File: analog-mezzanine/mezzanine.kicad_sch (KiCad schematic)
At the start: 16 parts, among them J1 Conn_Coaxial, J2 Conn_Coaxial, J9 LD15P24A4GV00LF

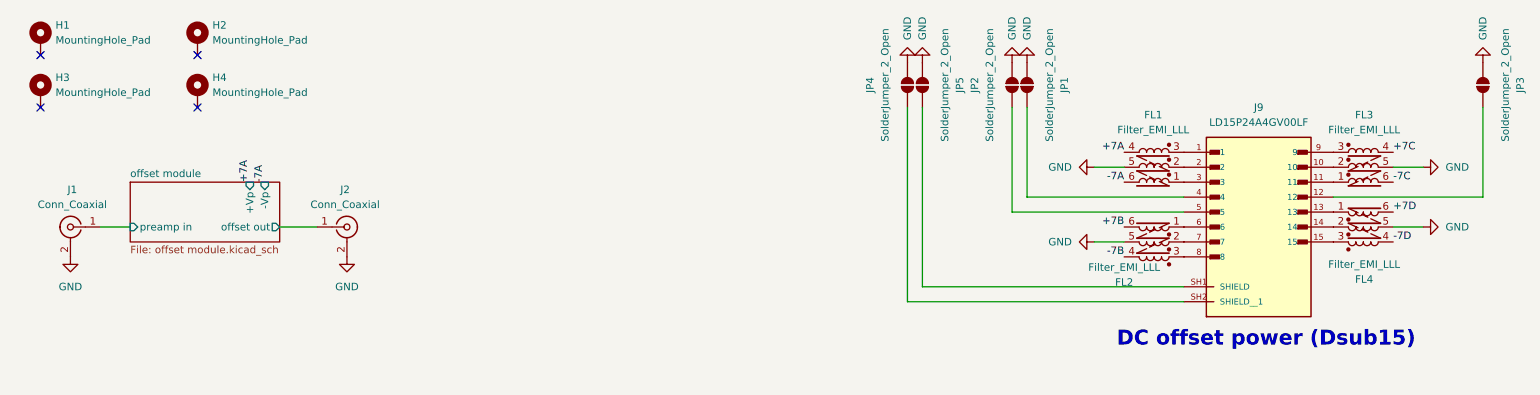
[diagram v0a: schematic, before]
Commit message: wire up linear regulators for offset
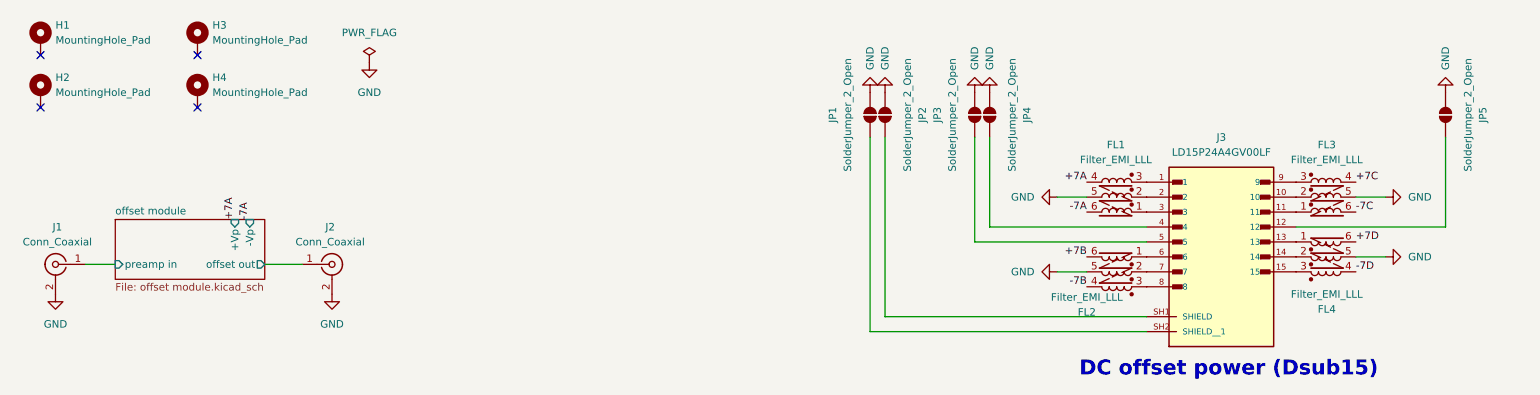
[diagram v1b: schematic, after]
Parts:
- renumbered H3 to H2, H2 to H3, J9 to J3, JP4 to JP1, JP5 to JP2, JP2 to JP3, JP1 to JP4, JP3 to JP5
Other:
- moved on the sheet: FL1, FL2, FL3, FL4, J1, J2, J3, JP1, JP2, JP3, JP4, JP5

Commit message: start layout
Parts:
- added J2, J3, J4: Conn_Coaxial, Connector_Coaxial:MMCX_Molex_73415-0961_Horizontal_1.0mm-PCB, symbol Connector:Conn_Coaxial
- added J6, J7, J8: Conn_Coaxial, Connector_Coaxial:MMCX_Molex_73415-1471_Vertical, symbol Connector:Conn_Coaxial
- J5: renamed from J2; footprint Connector_Coaxial:MMCX_Molex_73415-0961_Horizontal_1.0mm-PCB -> Connector_Coaxial:MMCX_Molex_73415-1471_Vertical
- JP1, JP2, JP3, JP4, JP5: footprint (none) -> Jumper:SolderJumper-2_P1.3mm_Open_RoundedPad1.0x1.5mm
- renumbered J3 to J9
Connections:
- net +7B: now also FL2.4 (2); no longer FL2.6
- net +7C: now also FL3.6; no longer FL3.4 (2)
- net -7B: now also FL2.6; no longer FL2.4 (2)
- net -7C: now also FL3.4 (2); no longer FL3.6
- net GND: now also J2.2 (Ext), J3.2 (Ext), J4.2 (Ext), J6.2 (Ext), J7.2 (Ext), J8.2 (Ext)
- net at FL3.1 (5): now also J9.9; no longer J9.11
- net at FL3.3 (1): now also J9.11; no longer J9.9
- net at FL2.1 (5): now also J9.8; no longer J9.6
- net at FL2.3 (1): now also J9.6; no longer J9.8
- new net offset module1/offset out: J6.1 (In)
- new net offset module1/preamp in: J2.1 (In)
- new net offset module2/offset out: J7.1 (In)
- new net offset module2/preamp in: J3.1 (In)
- new net offset module3/offset out: J8.1 (In)
- new net offset module3/preamp in: J4.1 (In)
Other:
- added sheet offset module1 (offset module.kicad_sch)
- added sheet offset module2 (offset module.kicad_sch)
- added sheet offset module3 (offset module.kicad_sch)
- moved on the sheet: FL2

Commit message: laid out chunks and power
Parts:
- J1, J2, J3, J4: footprint Connector_Coaxial:MMCX_Molex_73415-0961_Horizontal_1.0mm-PCB -> Connector_Coaxial:MMCX_Molex_73415-1471_Vertical

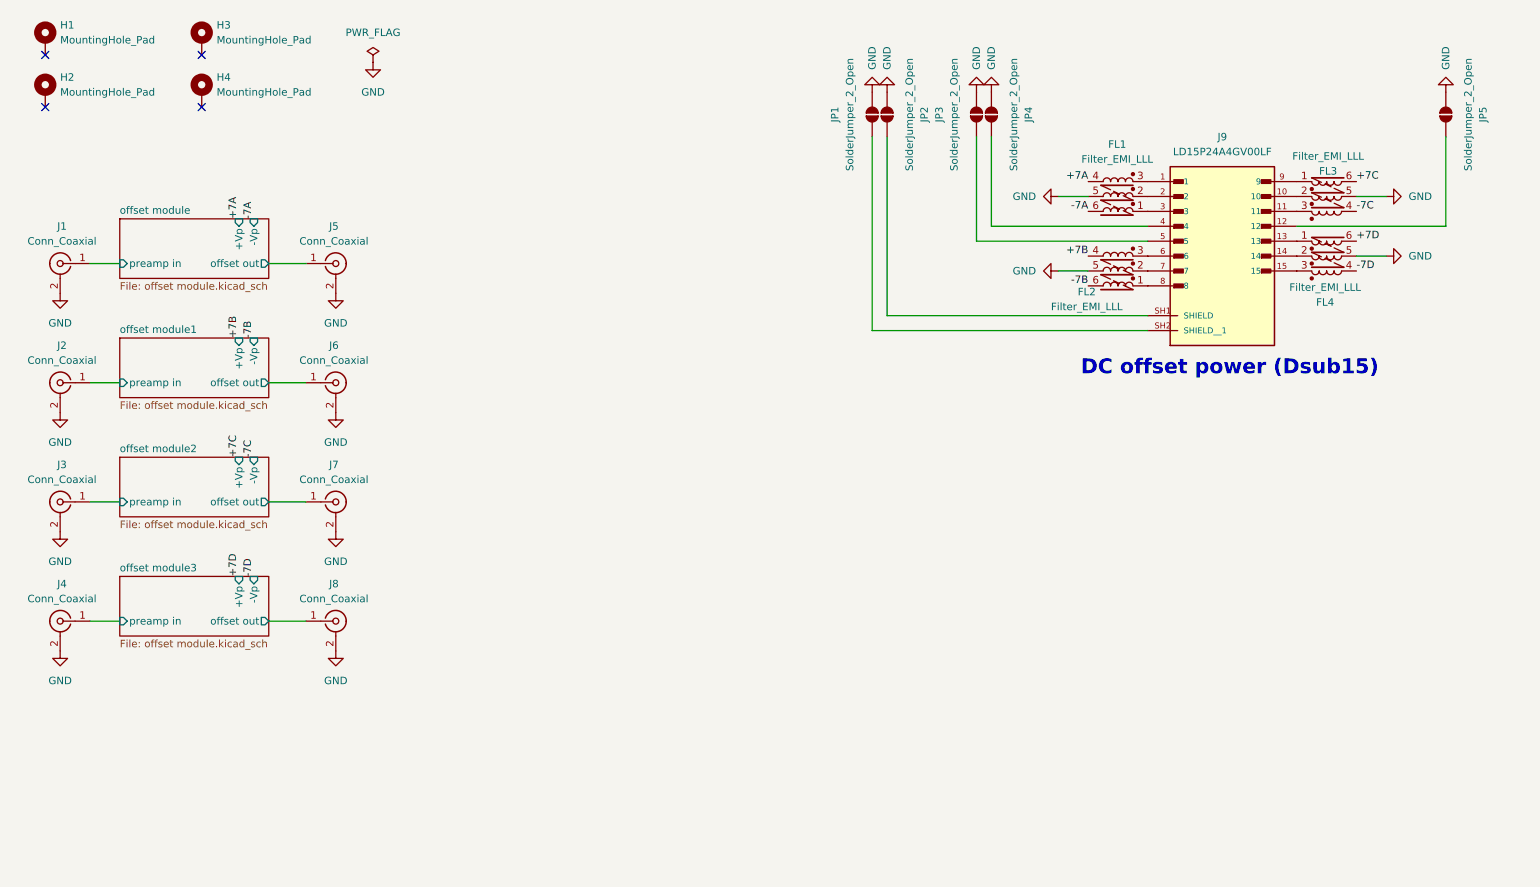
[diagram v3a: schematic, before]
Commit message: re-layout, better ground plane config
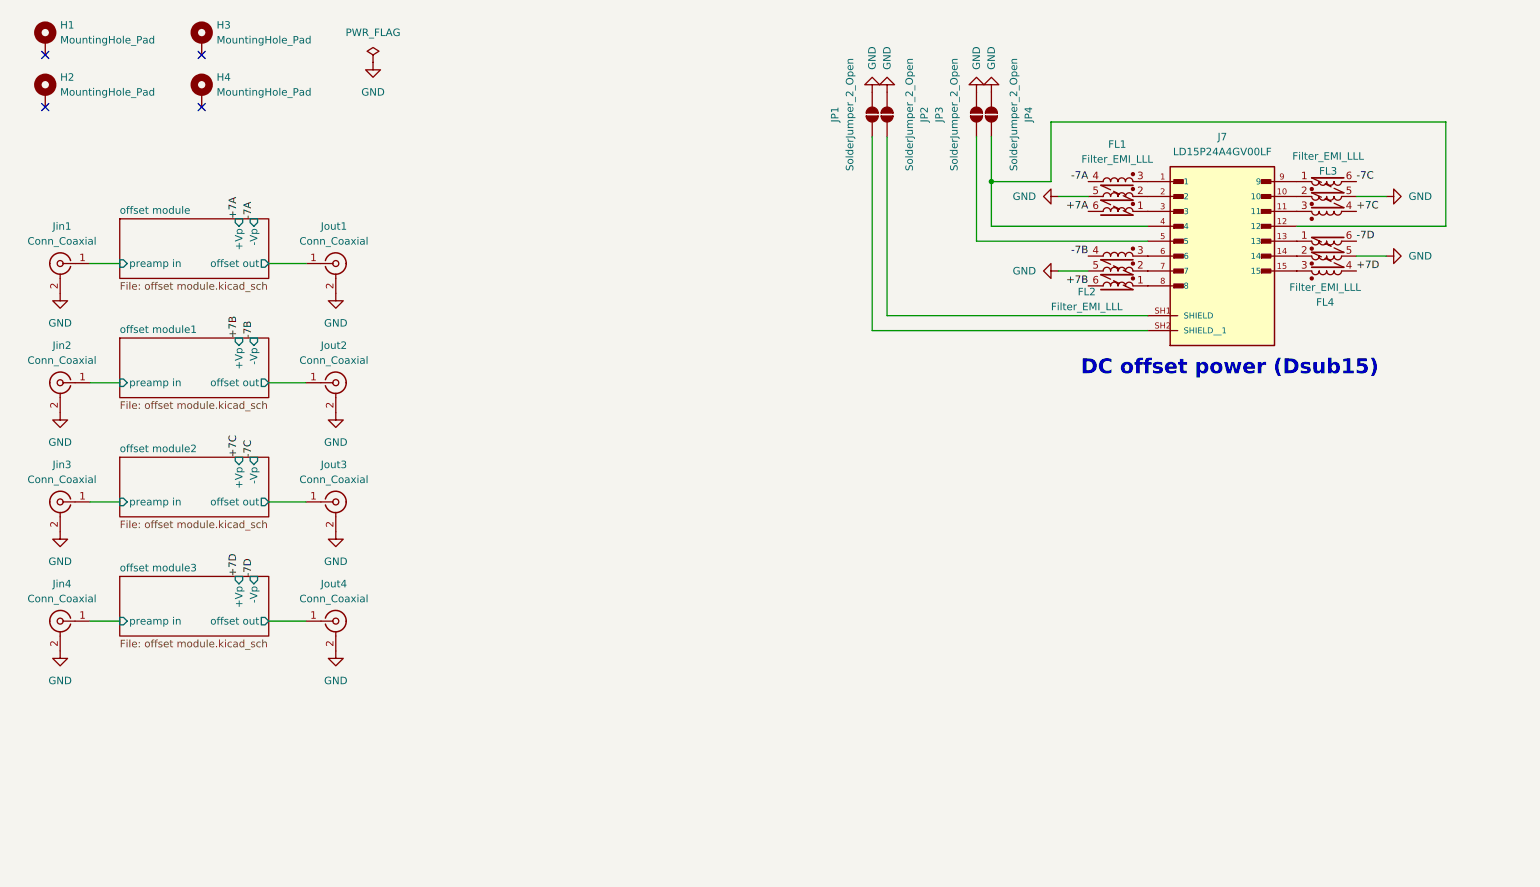
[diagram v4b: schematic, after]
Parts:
- removed JP5: SolderJumper_2_Open, Jumper:SolderJumper-2_P1.3mm_Open_RoundedPad1.0x1.5mm, symbol Jumper:SolderJumper_2_Open
- renumbered J9 to J7, J1 to Jin1, J2 to Jin2, J3 to Jin3, J4 to Jin4, J5 to Jout1, J6 to Jout2, J7 to Jout3, J8 to Jout4
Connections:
- net +7A: now also FL1.6; no longer FL1.4 (2)
- net +7B: now also FL2.6; no longer FL2.4 (2)
- net +7C: now also FL3.4 (2); no longer FL3.6
- net +7D: now also FL4.4 (2); no longer FL4.6
- net -7A: now also FL1.4 (2); no longer FL1.6
- net -7B: now also FL2.4 (2); no longer FL2.6
- net -7C: now also FL3.6; no longer FL3.4 (2)
- net -7D: now also FL4.6; no longer FL4.4 (2)
- net at J7.4, JP4.2 (B): now also J7.12
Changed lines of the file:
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@@
 		)
 	)
+	(junction
+		(at 189.23 45.72)
+		(diameter 0)
+		(color 0 0 0 0)
+	)
 	(no_connect
 		(at 27.94 33.02)
@@
 	(wire
 		(pts
+			(xy 266.7 35.56) (xy 199.39 35.56)
+		)
+		(stroke
+			(width 0)
+			(type default)
+		)
+	)
+	(wire
+		(pts
 			(xy 186.69 38.1) (xy 186.69 55.88)
 		)
@@
 	(wire
 		(pts
-			(xy 189.23 53.34) (xy 189.23 38.1)
+			(xy 189.23 53.34) (xy 189.23 45.72)
 		)
 		(stroke
@@
 	(wire
 		(pts
+			(xy 266.7 53.34) (xy 266.7 35.56)
+		)
+		(stroke
+			(width 0)
+			(type default)
+		)
+	)
+	(wire
+		(pts
+			(xy 189.23 45.72) (xy 189.23 38.1)
+		)
+		(stroke
+			(width 0)
+			(type default)
+		)
+	)
+	(wire
+		(pts
 			(xy 215.9 68.58) (xy 171.45 68.58)
 		)
@@
 	(wire
 		(pts
-			(xy 266.7 53.34) (xy 266.7 38.1)
+			(xy 199.39 45.72) (xy 189.23 45.72)
 		)
 		(stroke
@@
 	(wire
 		(pts
+			(xy 199.39 35.56) (xy 199.39 45.72)
+		)
+		(stroke
+			(width 0)
+			(type default)
+		)
+	)
+	(wire
+		(pts
 			(xy 200.66 48.26) (xy 205.74 48.26)
 		)
@@
 	)
 	(label "+7B"
-		(at 205.74 58.42 180)
+		(at 205.74 63.5 180)
 		(effects
 			(font
@@
 	)
 	(label "+7A"
-		(at 205.74 45.72 180)
+		(at 205.74 50.8 180)
 		(effects
 			(font
@@
 	)
 	(label "-7A"
-		(at 205.74 50.8 180)
+		(at 205.74 45.72 180)
 		(effects
 			(font
@@
 	)
 	(label "+7C"
-		(at 251.46 45.72 0)
+		(at 251.46 50.8 0)
 		(effects
 			(font
@@
 	)
 	(label "-7C"
-		(at 251.46 50.8 0)
+		(at 251.46 45.72 0)
 		(effects
 			(font
@@
 	)
 	(label "-7B"
-		(at 205.74 63.5 180)
+		(at 205.74 58.42 180)
 		(effects
 			(font
@@
 	)
 	(label "-7D"
-		(at 251.46 60.96 0)
+		(at 251.46 55.88 0)
 		(effects
 			(font
@@
 	)
 	(label "+7D"
-		(at 251.46 55.88 0)
+		(at 251.46 60.96 0)
 		(effects
 			(font
@@
 		(on_board yes)
 		(dnp no)
-		(property "Reference" "J5"
+		(property "Reference" "Jout1"
 			(at 77.1526 53.34 0)
 			(effects
@@
 			(project "dc-offsetter"
 				(path "/beaf6512-ab3f-4084-8005-c7f9afb6bef5"
-					(reference "J5")
+					(reference "Jout1")
 					(unit 1)
 				)
@@
 		(on_board yes)
 		(dnp no)
-		(property "Reference" "J4"
+		(property "Reference" "Jin4"
 			(at 30.7974 114.3 0)
 			(effects
@@
 			(project "mezzanine"
 				(path "/beaf6512-ab3f-4084-8005-c7f9afb6bef5"
-					(reference "J4")
+					(reference "Jin4")
 					(unit 1)
 				)
@@
 	)
 	(symbol
+		(lib_name "Filter_EMI_LLL_3")
 		(lib_id "Device:Filter_EMI_LLL")
 		(at 246.38 48.26 0)
@@
 		(on_board yes)
 		(dnp no)
-		(property "Reference" "J7"
+		(property "Reference" "Jout3"
 			(at 77.1526 93.98 0)
 			(effects
@@
 			(project "mezzanine"
 				(path "/beaf6512-ab3f-4084-8005-c7f9afb6bef5"
-					(reference "J7")
+					(reference "Jout3")
 					(unit 1)
 				)
@@
 		(on_board yes)
 		(dnp no)
-		(property "Reference" "J6"
+		(property "Reference" "Jout2"
 			(at 77.1526 73.66 0)
 			(effects
@@
 			(project "mezzanine"
 				(path "/beaf6512-ab3f-4084-8005-c7f9afb6bef5"
-					(reference "J6")
+					(reference "Jout2")
 					(unit 1)
 				)
@@
 		(on_board yes)
 		(dnp no)
-		(property "Reference" "J3"
+		(property "Reference" "Jin3"
 			(at 30.7974 93.98 0)
 			(effects
@@
 			(project "mezzanine"
 				(path "/beaf6512-ab3f-4084-8005-c7f9afb6bef5"
-					(reference "J3")
+					(reference "Jin3")
 					(unit 1)
 				)
@@
 	)
 	(symbol
+		(lib_name "Filter_EMI_LLL_2")
 		(lib_id "Device:Filter_EMI_LLL")
 		(at 210.82 60.96 0)
@@
 		(on_board yes)
 		(dnp no)
-		(property "Reference" "J1"
+		(property "Reference" "Jin1"
 			(at 30.7974 53.34 0)
 			(effects
@@
 			(project "mezzanine"
 				(path "/beaf6512-ab3f-4084-8005-c7f9afb6bef5"
-					(reference "J1")
+					(reference "Jin1")
 					(unit 1)
 				)
@@
 	)
 	(symbol
-		(lib_id "Jumper:SolderJumper_2_Open")
-		(at 266.7 34.29 90)
-		(mirror x)
-		(unit 1)
-		(exclude_from_sim no)
-		(in_bom no)
-		(on_board yes)
-		(dnp no)
-		(property "Reference" "JP5"
-			(at 273.05 34.29 0)
-			(effects
-				(font
-					(size 1.27 1.27)
-				)
-			)
-		)
-		(property "Value" "SolderJumper_2_Open"
-			(at 270.51 34.29 0)
-			(effects
-				(font
-					(size 1.27 1.27)
-				)
-			)
-		)
-		(property "Footprint" "Jumper:SolderJumper-2_P1.3mm_Open_RoundedPad1.0x1.5mm"
-			(at 266.7 34.29 0)
-			(effects
-				(font
-					(size 1.27 1.27)
-				)
-				(hide yes)
-			)
-		)
-		(property "Datasheet" "~"
-			(at 266.7 34.29 0)
-			(effects
-				(font
-					(size 1.27 1.27)
-				)
-				(hide yes)
-			)
-		)
-		(property "Description" "Solder Jumper, 2-pole, open"
-			(at 266.7 34.29 0)
-			(effects
-				(font
-					(size 1.27 1.27)
-				)
-				(hide yes)
-			)
-		)
-		(pin "1"
-		)
-		(pin "2"
-		)
-		(instances
-			(project "mezzanine"
-				(path "/beaf6512-ab3f-4084-8005-c7f9afb6bef5"
-					(reference "JP5")
-					(unit 1)
-				)
-			)
-		)
-	)
-	(symbol
 		(lib_id "power:GND")
 		(at 77.47 105.41 0)
@@
 	)
 	(symbol
+		(lib_name "Filter_EMI_LLL_1")
 		(lib_id "Device:Filter_EMI_LLL")
 		(at 210.82 48.26 0)
@@
 		(on_board yes)
 		(dnp no)
-		(property "Reference" "J2"
+		(property "Reference" "Jin2"
 			(at 30.7974 73.66 0)
 			(effects
@@
 			(project "mezzanine"
 				(path "/beaf6512-ab3f-4084-8005-c7f9afb6bef5"
-					(reference "J2")
-					(unit 1)
-				)
-			)
-		)
-	)
-	(symbol
-		(lib_id "power:GND")
-		(at 266.7 30.48 180)
-		(unit 1)
-		(exclude_from_sim no)
-		(in_bom yes)
-		(on_board yes)
-		(dnp no)
-		(fields_autoplaced yes)
-		(property "Reference" "#PWR018"
-			(at 266.7 24.13 0)
-			(effects
-				(font
-					(size 1.27 1.27)
-				)
-				(hide yes)
-			)
-		)
-		(property "Value" "GND"
-			(at 266.7001 26.67 90)
-			(effects
-				(font
-					(size 1.27 1.27)
-				)
-				(justify right)
-			)
-		)
-		(property "Footprint" ""
-			(at 266.7 30.48 0)
-			(effects
-				(font
-					(size 1.27 1.27)
-				)
-				(hide yes)
-			)
-		)
-		(property "Datasheet" ""
-			(at 266.7 30.48 0)
-			(effects
-				(font
-					(size 1.27 1.27)
-				)
-				(hide yes)
-			)
-		)
-		(property "Description" "Power symbol creates a global label with name \"GND\" , ground"
-			(at 266.7 30.48 0)
-			(effects
-				(font
-					(size 1.27 1.27)
-				)
-				(hide yes)
-			)
-		)
-		(pin "1"
-		)
-		(instances
-			(project "dc-offsetter"
-				(path "/beaf6512-ab3f-4084-8005-c7f9afb6bef5"
-					(reference "#PWR018")
+					(reference "Jin2")
 					(unit 1)
 				)
@@
 		(dnp no)
 		(fields_autoplaced yes)
-		(property "Reference" "J9"
+		(property "Reference" "J7"
 			(at 228.6 38.1 0)
 			(effects
@@
 			(project ""
 				(path "/beaf6512-ab3f-4084-8005-c7f9afb6bef5"
-					(reference "J9")
+					(reference "J7")
 					(unit 1)
 				)
@@
 		(on_board yes)
 		(dnp no)
-		(property "Reference" "J8"
+		(property "Reference" "Jout4"
 			(at 77.1526 114.3 0)
 			(effects
@@
 			(project "mezzanine"
 				(path "/beaf6512-ab3f-4084-8005-c7f9afb6bef5"
-					(reference "J8")
+					(reference "Jout4")
 					(unit 1)
 				)

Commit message: update layout: central D connector
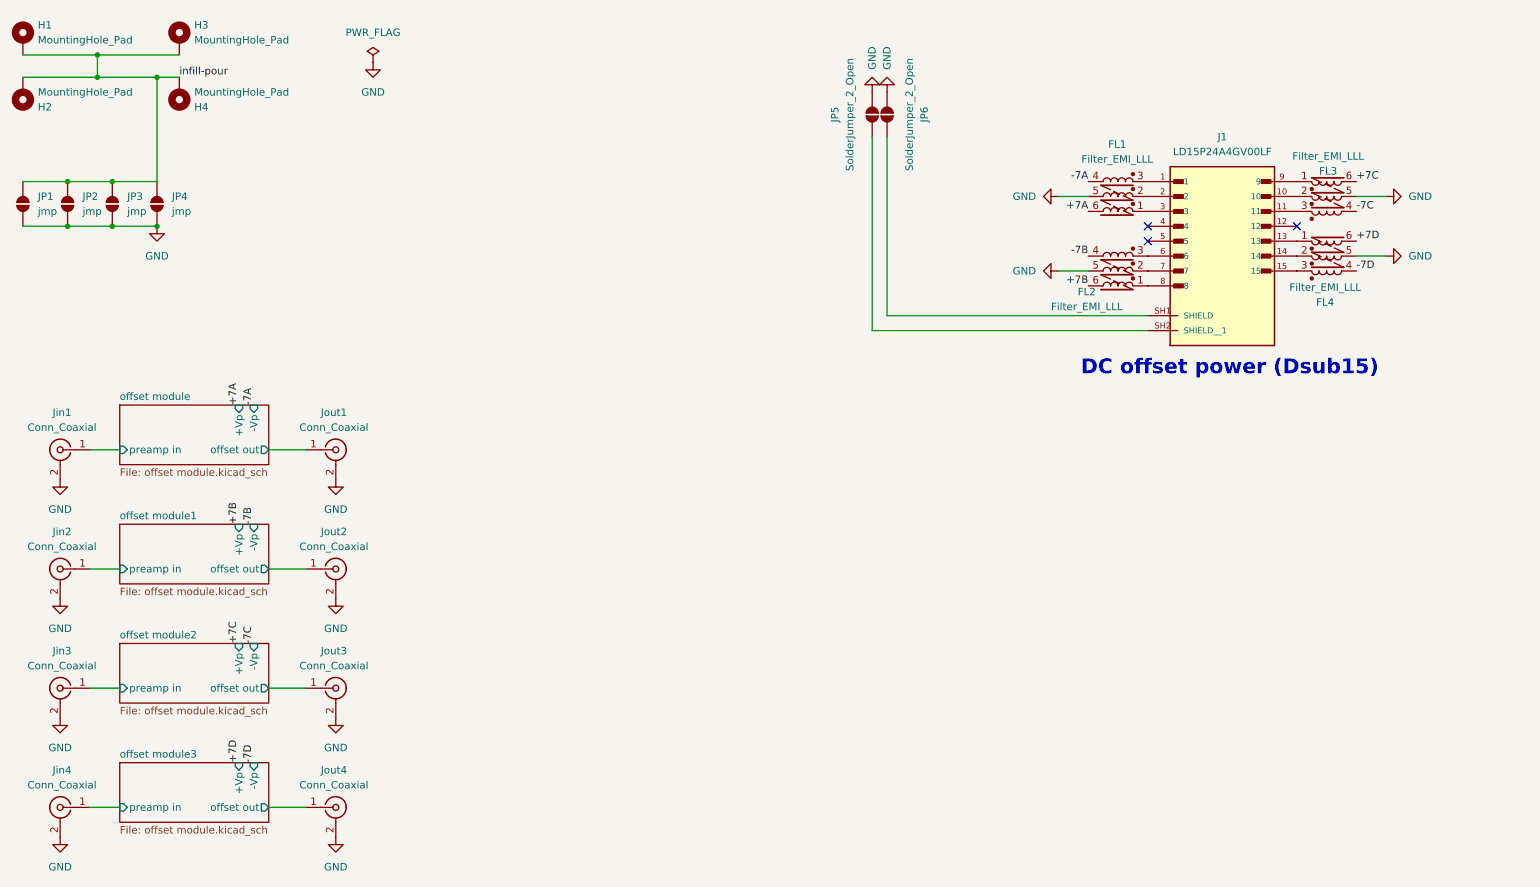
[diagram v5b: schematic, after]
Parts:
- added JP1, JP2: jmp, Jumper:SolderJumper-2_P1.3mm_Open_RoundedPad1.0x1.5mm, symbol Jumper:SolderJumper_2_Open
- JP3, JP4: value SolderJumper_2_Open -> jmp
- renumbered J7 to J1, JP1 to JP5, JP2 to JP6
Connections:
- net +7C: now also FL3.6; no longer FL3.4 (2)
- net +7D: now also FL4.6; no longer FL4.4 (2)
- net -7C: now also FL3.4 (2); no longer FL3.6
- net -7D: now also FL4.4 (2); no longer FL4.6
- net GND: now also JP1.1 (A), JP2.1 (A)
- net infill-pour: now reaches H1.1
- net infill-pour: now also H2.1, H3.1, H4.1, JP3.2 (B), JP4.2 (B), JP1.2 (B), JP2.2 (B)
- net at J1.5: no longer JP3.2 (B)
- now unconnected: J1.12, J1.4
- no-connect marks 4 -> 3
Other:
- moved on the sheet: H1, H2, H3, H4, Jin1, Jin2, Jin3, Jin4, Jout1, Jout2, Jout3, Jout4
